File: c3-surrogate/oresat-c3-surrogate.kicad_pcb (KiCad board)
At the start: 2 copper layers, 72 parts, among them J1 J-SAMTEC-TFM-120-X1-XXX-D-RA, J2 Conn_01x04, J4 PHOENIX_1995499, Q1 PMV45EN, Q3 NTR4101P, Q4 NTR4101P, Q5 DMP3050LVT-7, SW2 EG1218, SW3 OS203011MV9QS1, SW4 EG1218, U1 MAX892LEUA+T, U2 LTC4412xS6, U4 LTC4412xS6, U5 TS5A21366, U6 Trinket-M0

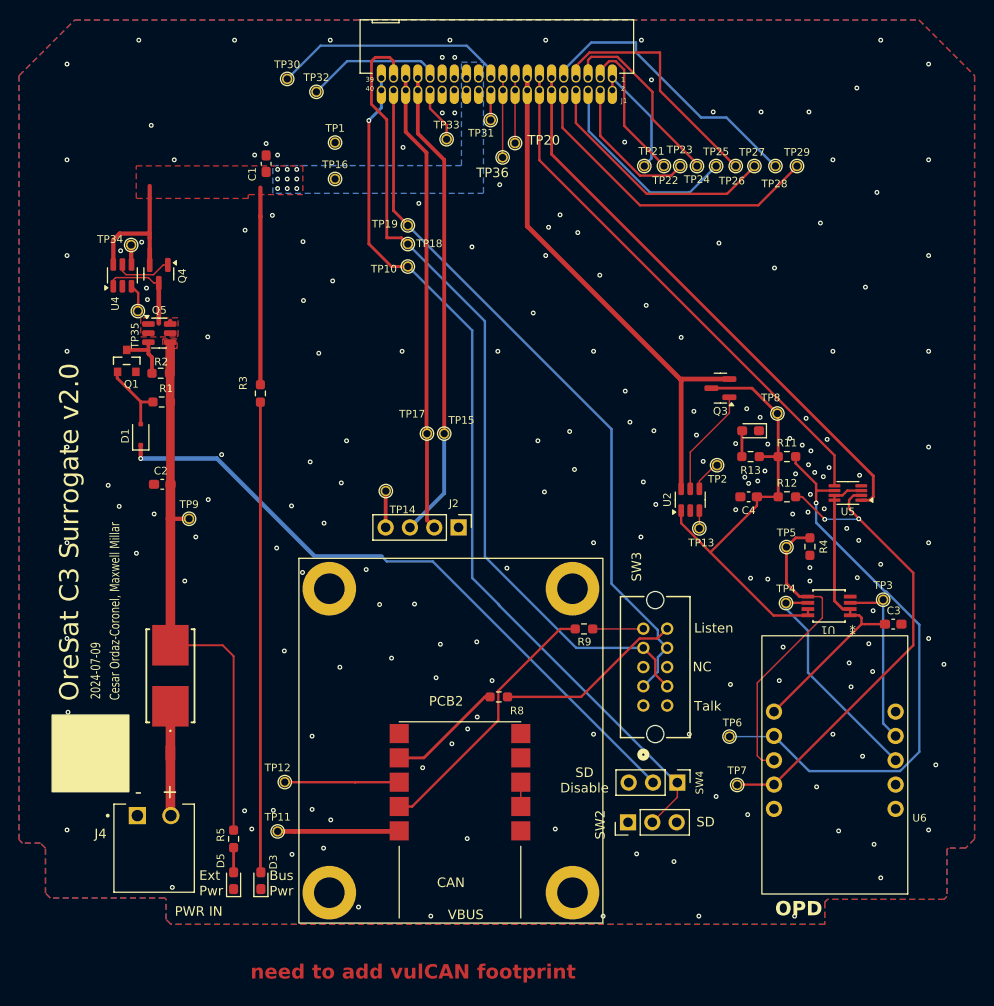
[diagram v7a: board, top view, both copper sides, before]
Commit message: Fix schematic, some polish, and began polishing layout.
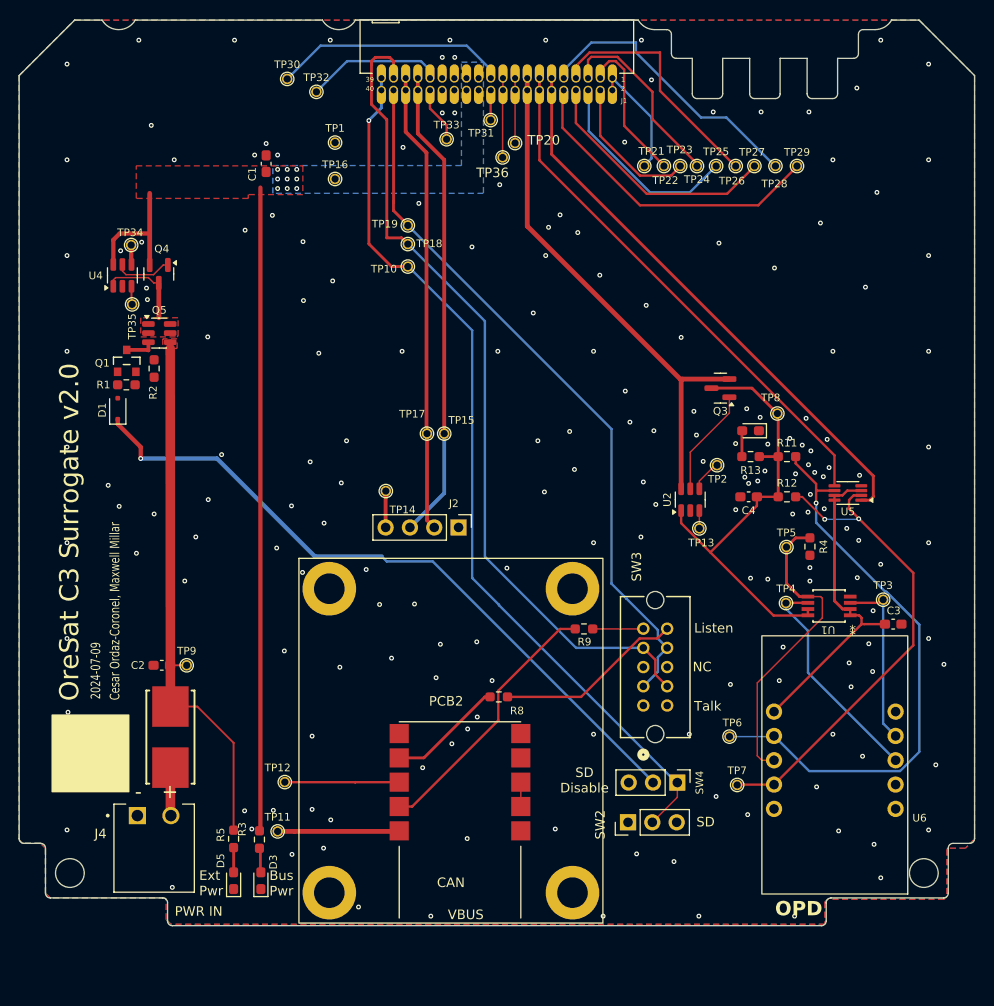
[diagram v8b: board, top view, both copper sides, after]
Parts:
- added PCB1: ORESAT-CARD-V1.3-GENERIC-3RF, oresat-pcbs:ORESAT-CARD-V1.3-3RF, F.Cu at (149.9, 100.2)
- moved R3 46.6 mm to (125.1, 141.0)
- moved C2 18.9 mm to (114.9, 122.8)
- moved TP9 15.3 mm to (117.5, 122.8)
- moved F2 6.41 mm to (115.8, 130.3)
- moved R1 4.10 mm to (111.2, 93.5)
- moved D1 3.61 mm to (110.3, 96.0)
- moved TP35 0.92 mm to (111.8, 85.1)
- moved R2 0.85 mm to (114.1, 91.8), turned to 90 degrees
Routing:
- net Net-(D3-A): track 49.2 -> 2.64 mm
- net VBUS: track 35.5 -> 81.4 mm
- net Net-(J4-Pin_2): track 12.8 -> 5.03 mm
- net Net-(D1-A): track 7.70 -> 0.00 mm
- net Net-(D1-K): track 69.0 -> 72.7 mm
- net Net-(Q1-D): track 5.68 -> 3.13 mm
- net Net-(U4-CTL): track 2.85 -> 1.92 mm
- net Net-(Q5-S): track 58.2 -> 57.5 mm
- net Net-(Q4-D): track 10.0 -> 9.38 mm
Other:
- board outline added: 99.8 x 94.6 mm
- board text removed: "need to add vulCAN footprint"
